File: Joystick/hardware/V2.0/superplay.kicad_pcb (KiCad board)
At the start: 4 copper layers, 36 parts, among them J1 AVR-PDI-6A, J2 CONN_02X04, J3 USB_B, U1 MCP1700T-3002E, U2 ATXMEGA128A3U-A, U3 TPD4S009DBV, Y1 16MHz

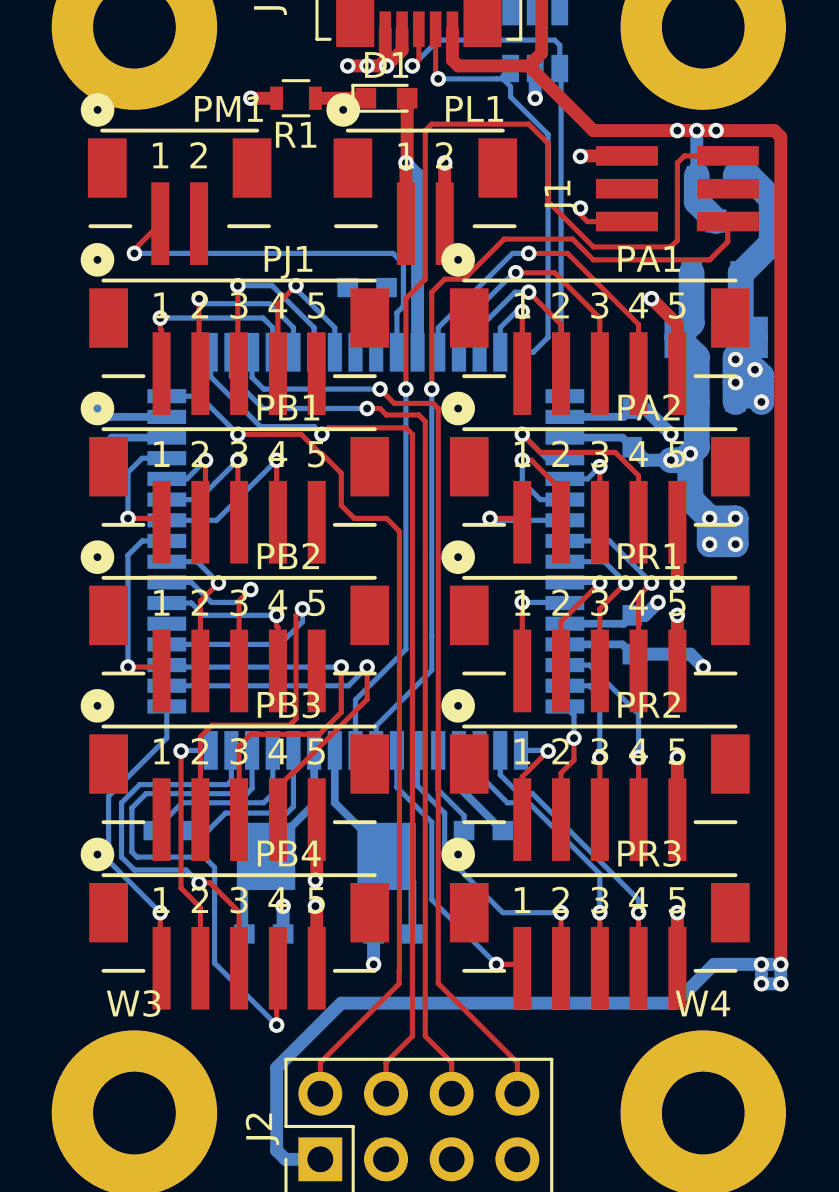
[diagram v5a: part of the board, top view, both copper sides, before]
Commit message: Routing finished, passes DRC
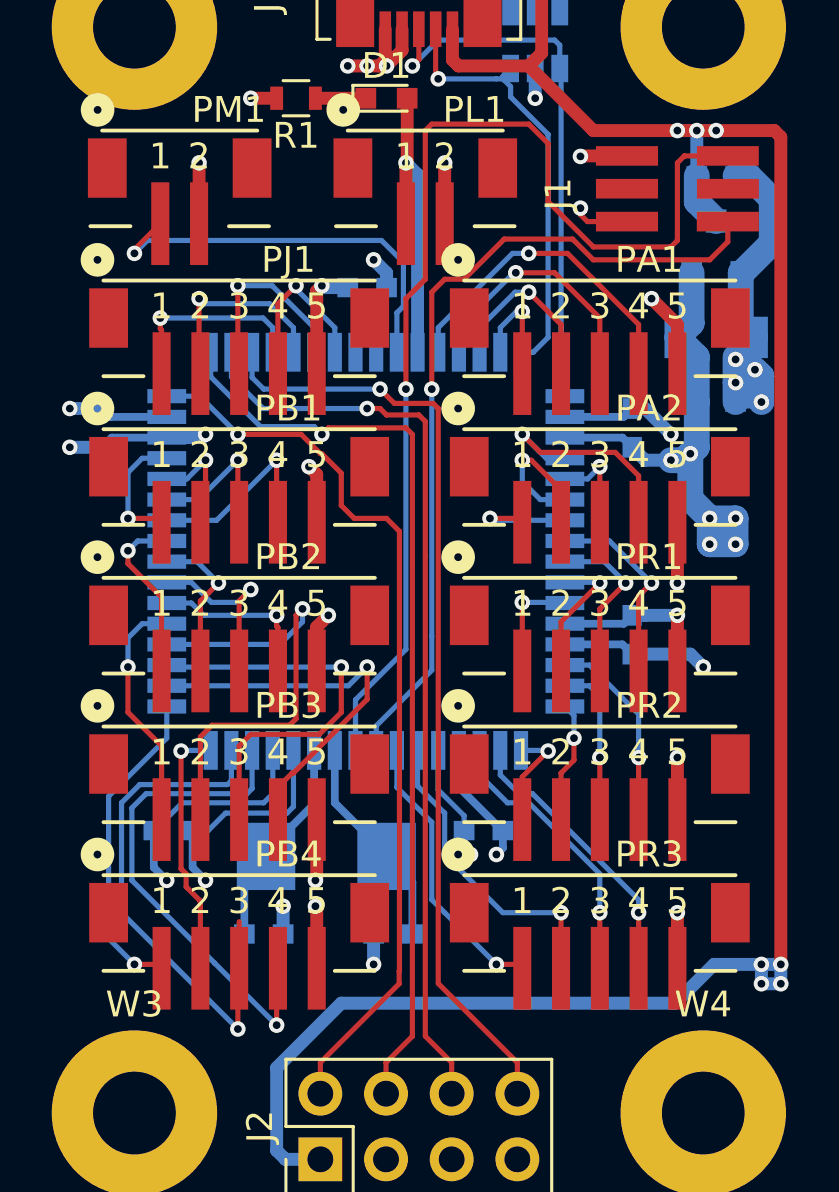
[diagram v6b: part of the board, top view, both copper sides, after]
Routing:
- net GND: track 68.6 -> 86.5 mm, vias 22 -> 29
- net /B9: track 0.00 -> 9.29 mm, vias 0 -> 1
- net +3V3: track 43.3 -> 49.0 mm, vias 8 -> 12
- net /B15: track 15.5 -> 20.6 mm
- net /B16: track 20.9 -> 19.4 mm
- net /B13: track 11.9 -> 12.5 mm

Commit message: Silkscreens
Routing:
- net GND: track 86.5 -> 87.1 mm
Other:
- board text added: "1"
- board text added: "C1"
- board text added: "C10"
- board text added: "C11"
- board text added: "C2"
- board text added: "C3"
- board text added: "C4"
- board text added: "C5"
- board text added: "C6"
- board text added: "C7"
- board text added: "C8"
- board text added: "C9"
- board text added: "J2"
- board text added: "U1"
- board text added: "U2"
- board text added: "U3"
- board text added: "Y1"
